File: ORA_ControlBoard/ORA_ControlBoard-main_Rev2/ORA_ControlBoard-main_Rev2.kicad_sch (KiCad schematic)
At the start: 69 parts, among them J1 SM04B-GHS-TB, J2 Conn_01x04_Pin, J3 USB_B_Micro, J4 12V, J5 SM04B-GHS-TB, J6 Conn_02x03_Top_Bottom, J7 Conn_01x05_Pin, J8 Conn_01x05_Pin, J9 Stack Light, Q1 BS170, Q2 IRF9540N, Q3 BS170, Q4 IRF9540N, Q5 BS170, Q6 IRF9540N, SW1 Reset, U1 ATmega32U4-A, U2 MCP25625-x-SS, U5 NCP1117-5.0_SOT223, U6 IMU_MOUNT, Y1 8Mhz, Y2 16MHz

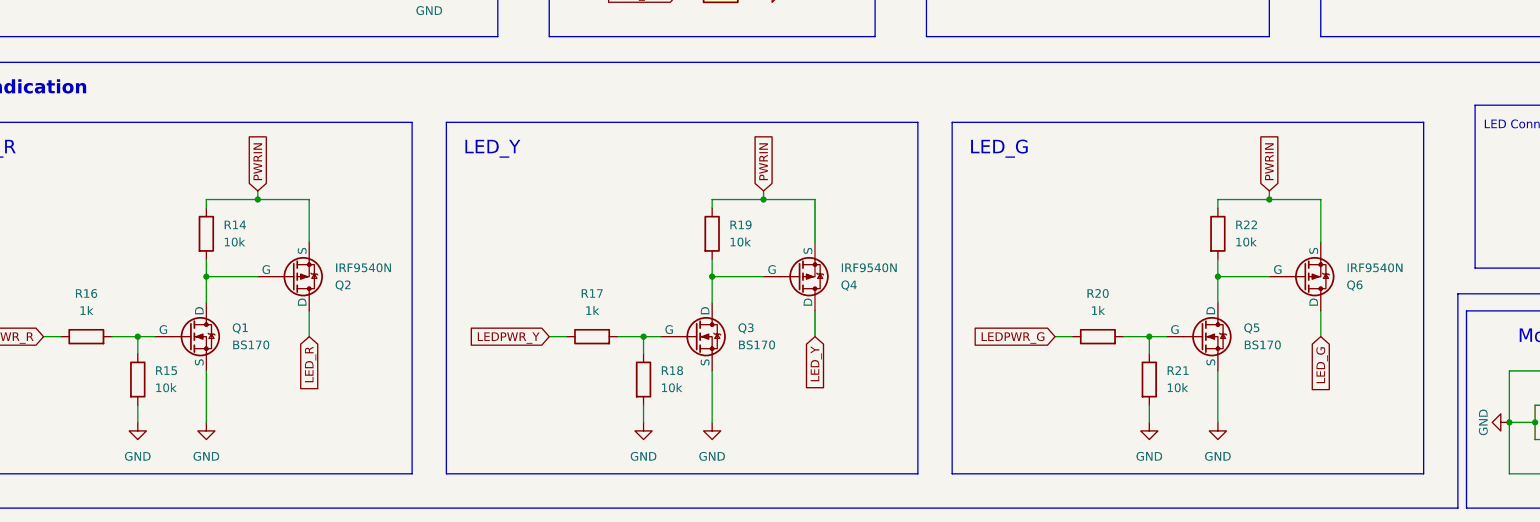
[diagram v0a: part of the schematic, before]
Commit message: Updated LED circuit
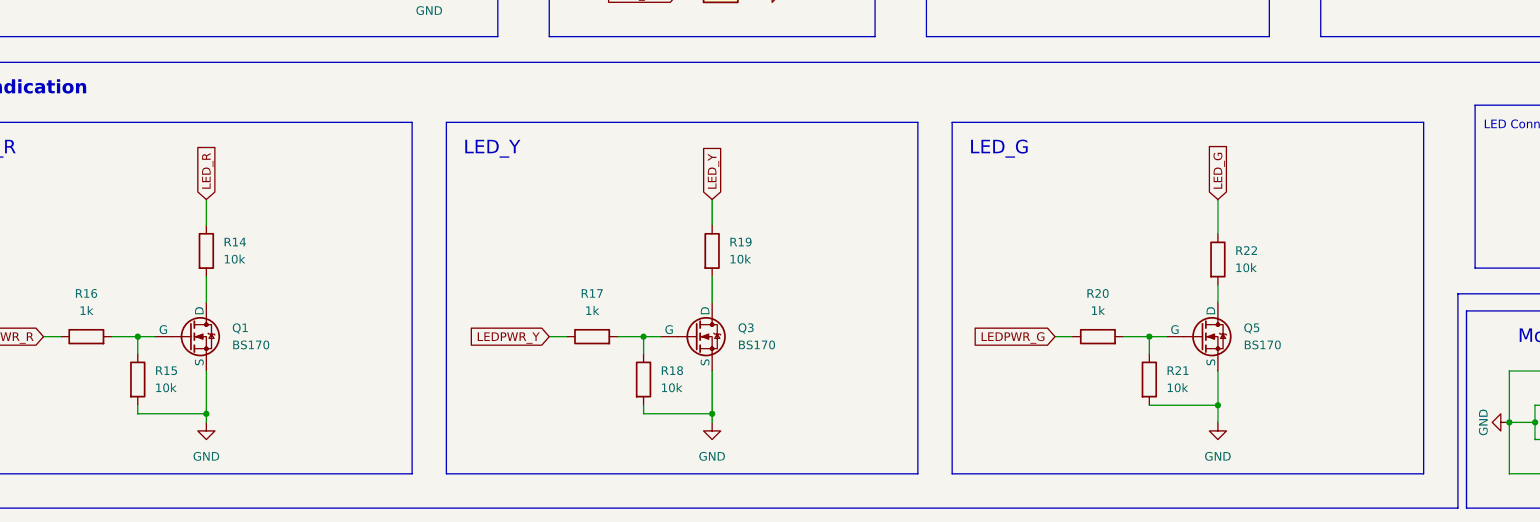
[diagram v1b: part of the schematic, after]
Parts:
- removed Q2, Q4, Q6: IRF9540N, Package_TO_SOT_THT:TO-220-3_Vertical, symbol Simulation_SPICE:PMOS
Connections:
- net LED_G: now also R22.1
- net LED_R: now also R14.1
- net LED_Y: now also R19.1
- net PWRIN: no longer R14.1, R19.1, R22.1
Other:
- moved on the sheet: R14, R19, R22

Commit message: Fixed Spring Cleaning
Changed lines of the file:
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@@
 	(wire
 		(pts
+			(xy 187.96 140.97) (xy 193.04 140.97)
+		)
+		(stroke
+			(width 0)
+			(type default)
+		)
+	)
+	(wire
+		(pts
 			(xy 287.02 101.6) (xy 280.67 101.6)
 		)
@@
 	(wire
 		(pts
+			(xy 187.96 138.43) (xy 193.04 138.43)
+		)
+		(stroke
+			(width 0)
+			(type default)
+		)
+	)
+	(wire
+		(pts
 			(xy 54.61 213.36) (xy 54.61 214.63)
 		)
@@
 	(wire
 		(pts
+			(xy 187.96 135.89) (xy 193.04 135.89)
+		)
+		(stroke
+			(width 0)
+			(type default)
+		)
+	)
+	(wire
+		(pts
 			(xy 266.7 78.74) (xy 262.89 78.74)
 		)
@@
 	(global_label "PWRIN"
 		(shape input)
-		(at 193.04 135.89 180)
+		(at 187.96 135.89 180)
 		(fields_autoplaced yes)
 		(effects
@@
 		)
 		(property "Intersheetrefs" "${INTERSHEET_REFS}"
-			(at 184.1281 135.89 0)
+			(at 179.0481 135.89 0)
 			(effects
 				(font
@@
 	(global_label "CAN_L"
 		(shape input)
-		(at 193.04 140.97 180)
+		(at 187.96 140.97 180)
 		(fields_autoplaced yes)
 		(effects
@@
 		)
 		(property "Intersheetrefs" "${INTERSHEET_REFS}"
-			(at 184.37 140.97 0)
+			(at 179.29 140.97 0)
 			(effects
 				(font
@@
 	(global_label "CAN_H"
 		(shape input)
-		(at 193.04 138.43 180)
+		(at 187.96 138.43 180)
 		(fields_autoplaced yes)
 		(effects
@@
 		)
 		(property "Intersheetrefs" "${INTERSHEET_REFS}"
-			(at 184.0676 138.43 0)
+			(at 178.9876 138.43 0)
 			(effects
 				(font

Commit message: "Final" Rev 2 changes
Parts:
- removed D5: IMU_LED, LED_SMD:LED_0805_2012Metric_Pad1.15x1.40mm_HandSolder, symbol Device:LED_Small
- removed R7: 470, Resistor_SMD:R_0805_2012Metric_Pad1.20x1.40mm_HandSolder, symbol Device:R_Small
- J3: footprint Connector_USB:USB_Micro-B_Amphenol_10118193-0002LF_Horizontal -> AdditionalParts:AMPHENOL_10118192-0002LF
- renumbered R1 to TR1
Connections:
- net LEDPWR_Y is gone; now on net LEDPWR_G: R17.1, U1.26 (PD6)
- net LED_Y is gone; now on net LED_G: J9.3 (Pin_3), R19.1
- net +5V: now also C7.1, U1.7 (VBUS)
- net GND: no longer J9.1 (Pin_1)
- net LEDPWR_G: no longer R20.1, U1.27 (PD7)
- net LED_G: no longer J9.2 (Pin_2), R22.1
- net LED_R: now also J9.2 (Pin_2); no longer J9.4 (Pin_4)
- net PWRIN: now also J9.1 (Pin_1)
- net at D3.2 (A), F1.2: no longer J3.1 (VBUS)
- removed net VBUS: C7.1, F1.1, U1.7 (VBUS)
- new net: F1.1, J3.1 (VBUS)
- new net LEDPWR_B: R20.1, U1.27 (PD7)
- new net LED_B: J9.4 (Pin_4), R22.1
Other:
- note added: "LED_B"
- note removed: "LED_Y"
- moved on the sheet: C11, C12, C13, C14, D3, D4, J3, J4, Q1, Q3, Q5, R14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

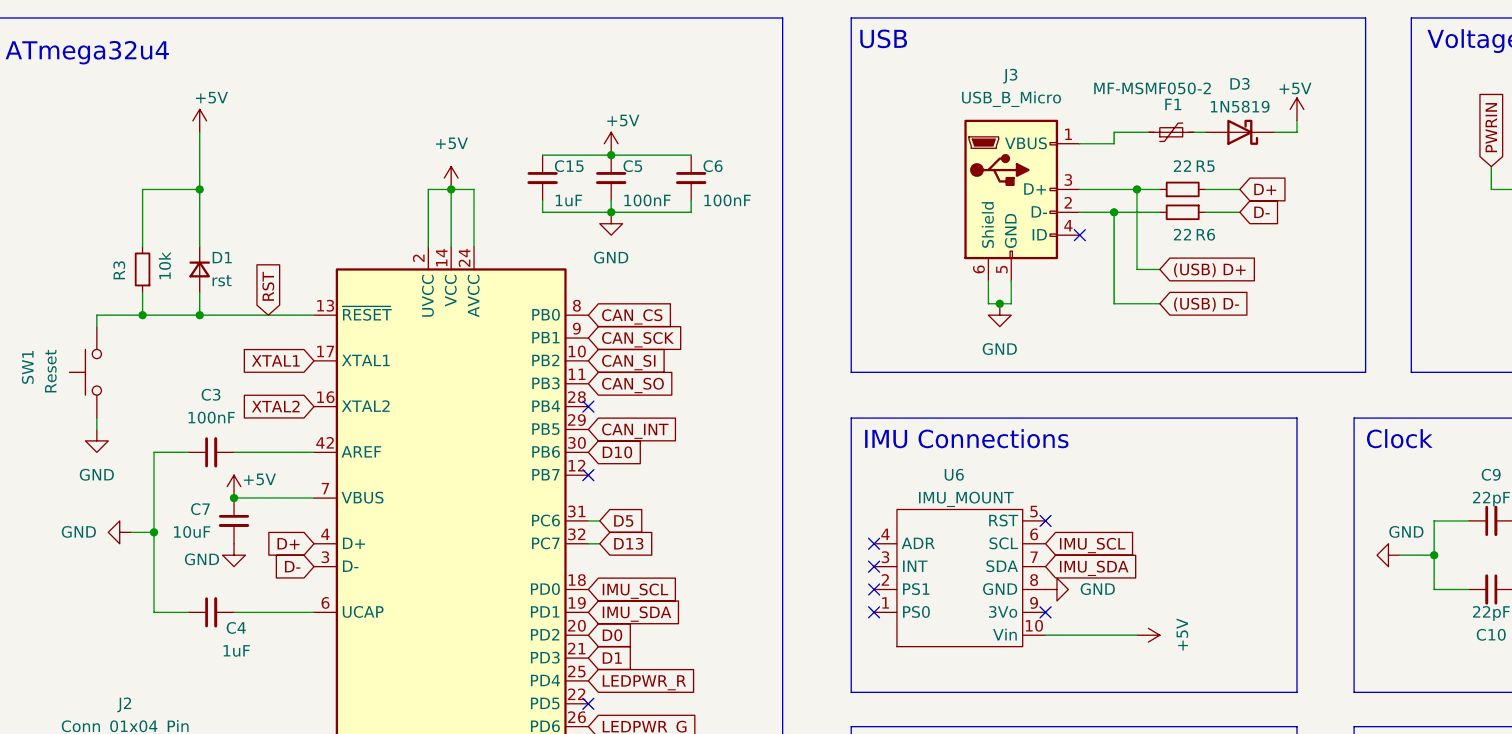
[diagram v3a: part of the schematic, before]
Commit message: Revision
Things changed:
VBUS flag added in between fuse and schottky diode (check this)
Got rid of C7 and GND to VBUS pin on ATmega
Changed silkscreen for ISP pins
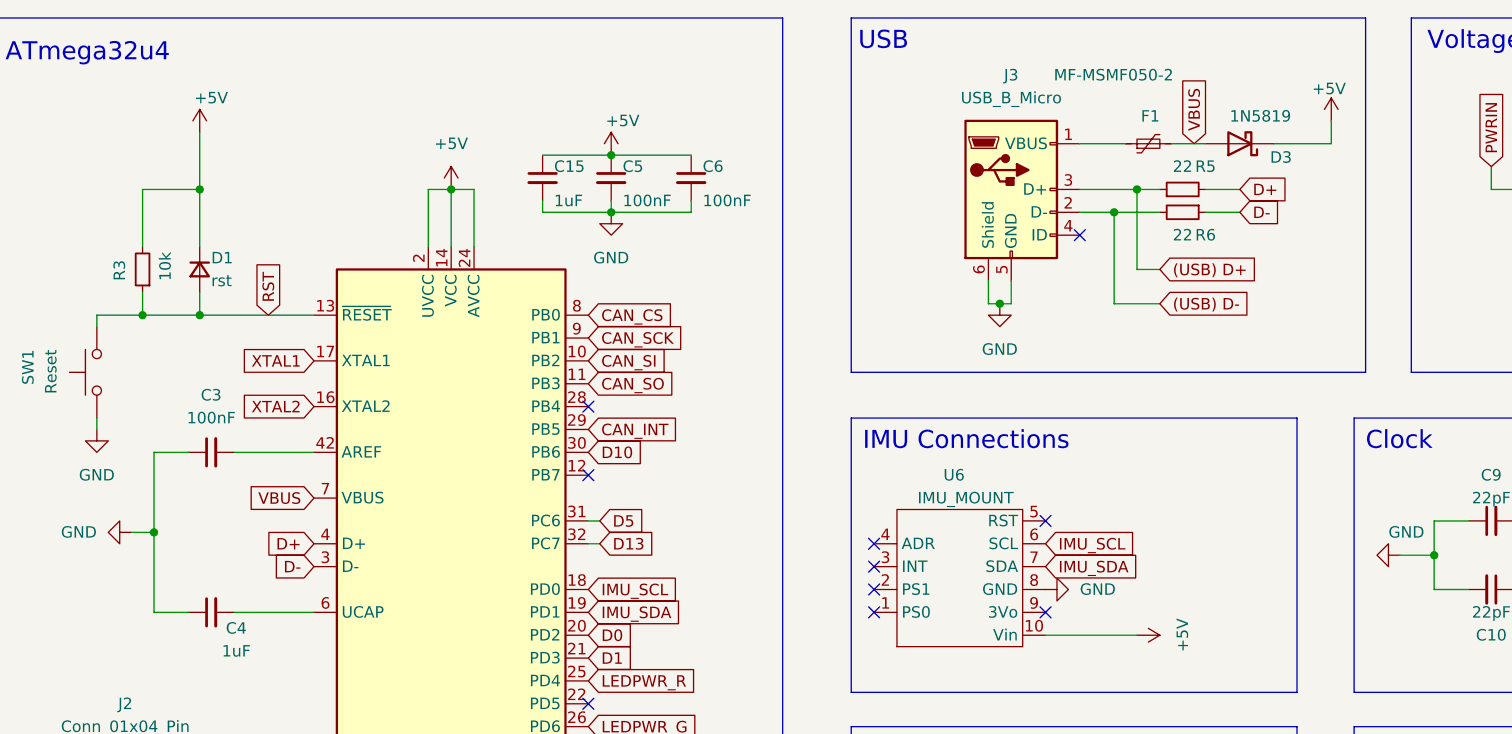
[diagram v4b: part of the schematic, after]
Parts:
- removed C7: 10uF, Capacitor_SMD:C_0805_2012Metric_Pad1.18x1.45mm_HandSolder, symbol Device:C_Small
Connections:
- net +5V: no longer U1.7 (VBUS)
- net VBUS: now reaches D3.2 (A), F1.2
- net VBUS: now also U1.7 (VBUS)
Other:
- moved on the sheet: D3, F1

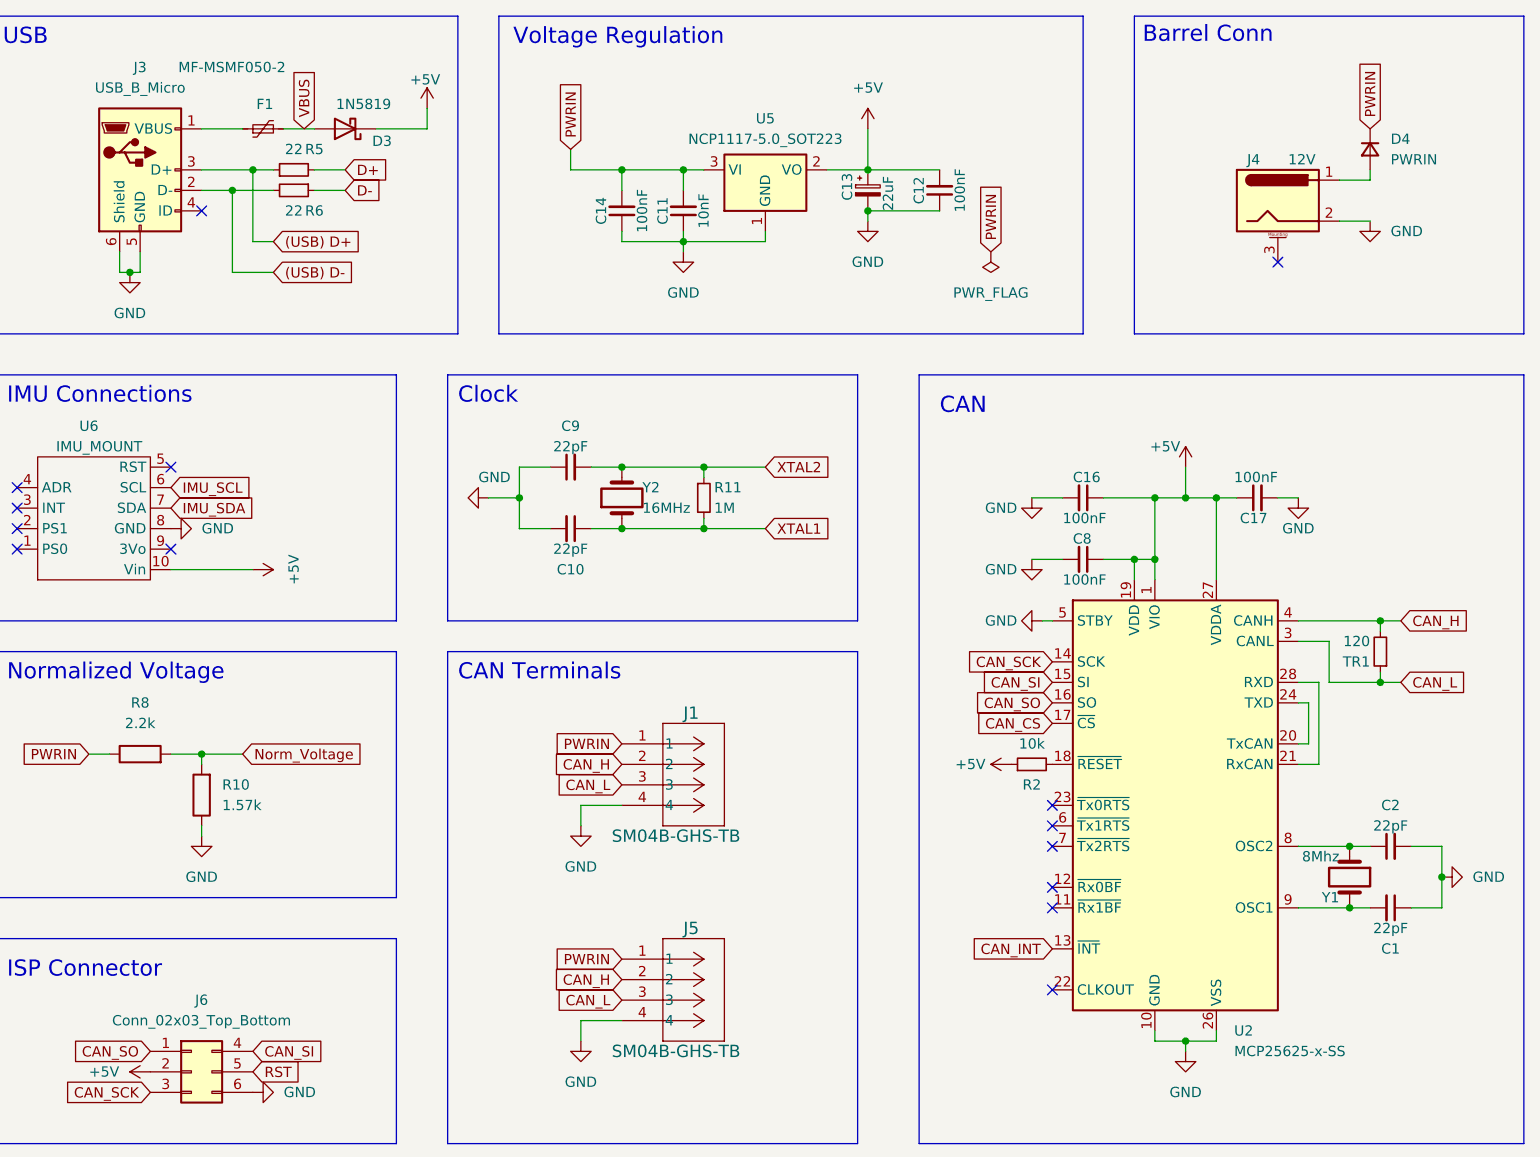
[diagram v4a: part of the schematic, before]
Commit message: Rev 2.1
Things changed:
VBUS flag added in between fuse and schottky diode

Got rid of C7 and GND to VBUS pin on ATmega

Make CAN_H and CAN_L traces differential pairs
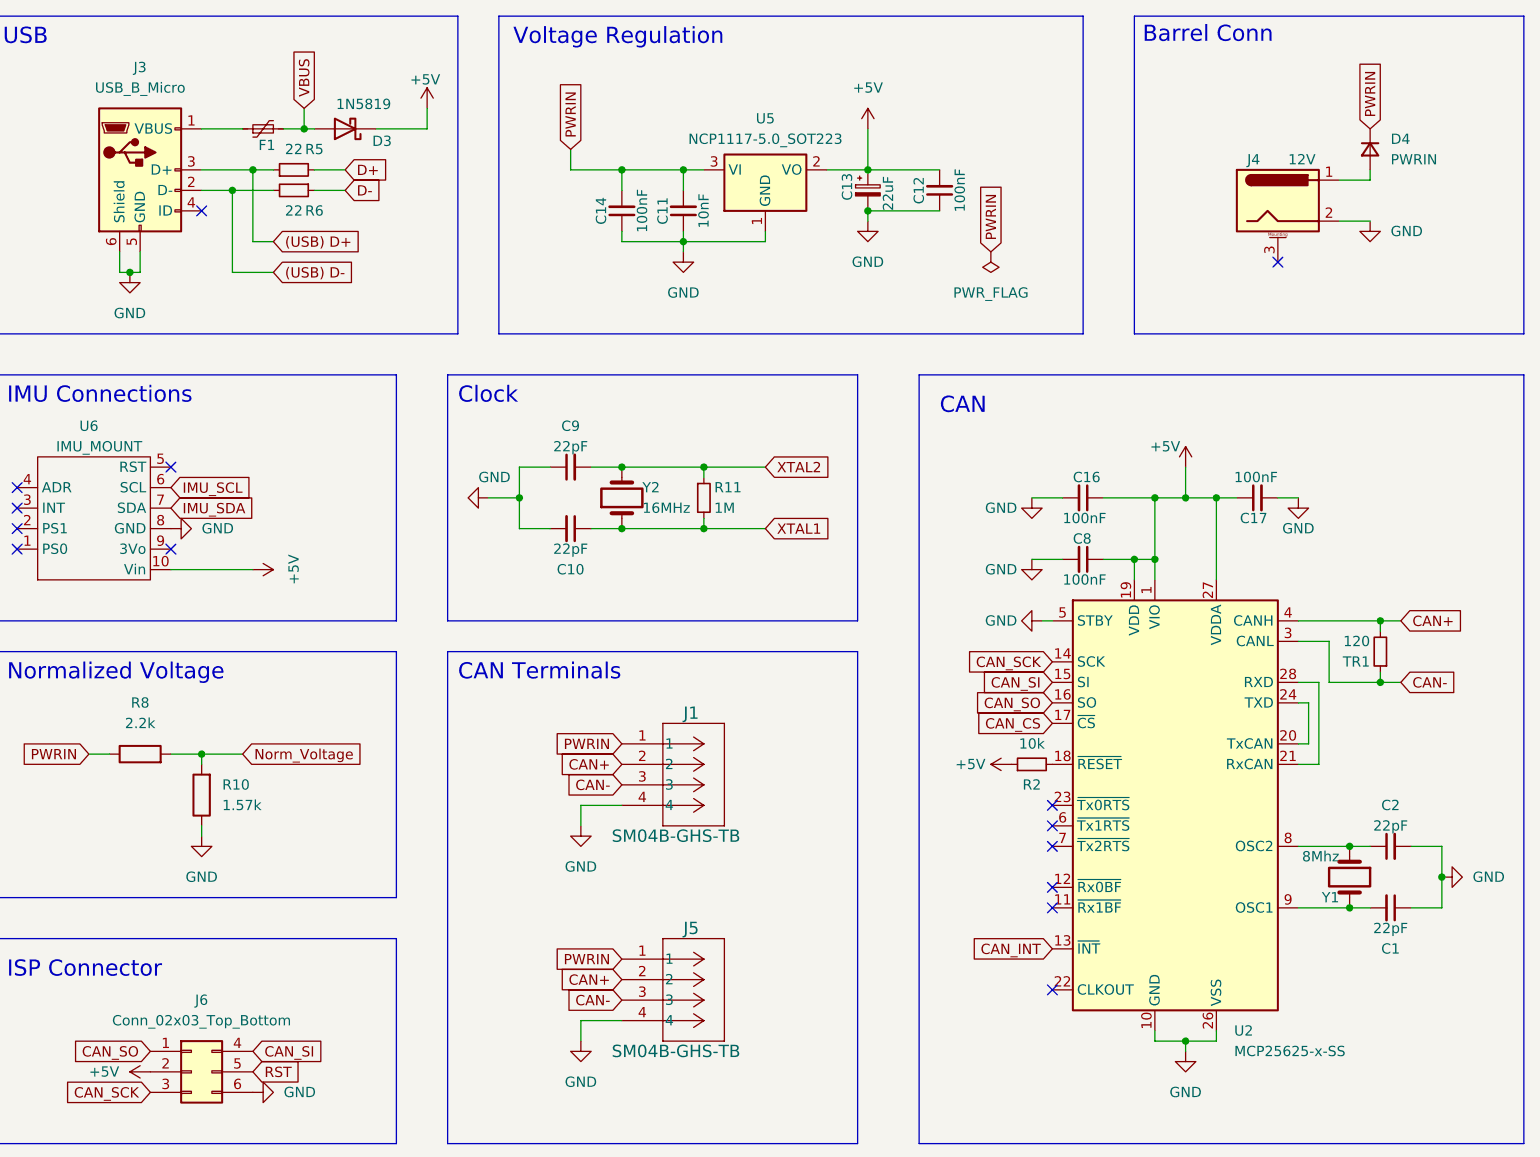
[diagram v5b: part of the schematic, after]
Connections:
- net CAN_H renamed CAN+
- net CAN_L renamed CAN-
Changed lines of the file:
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@@
 	)
 	(junction
+		(at 153.67 33.02)
+		(diameter 0)
+		(color 0 0 0 0)
+	)
+	(junction
 		(at 283.21 121.92)
 		(diameter 0)
@@
 	(wire
 		(pts
+			(xy 153.67 33.02) (xy 154.94 33.02)
+		)
+		(stroke
+			(width 0)
+			(type default)
+		)
+	)
+	(wire
+		(pts
 			(xy 68.58 138.43) (xy 69.85 138.43)
 		)
@@
 	(wire
 		(pts
+			(xy 151.13 33.02) (xy 153.67 33.02)
+		)
+		(stroke
+			(width 0)
+			(type default)
+		)
+	)
+	(wire
+		(pts
 			(xy 276.86 104.14) (xy 278.13 104.14)
 		)
@@
 	(wire
 		(pts
+			(xy 153.67 30.48) (xy 153.67 33.02)
+		)
+		(stroke
+			(width 0)
+			(type default)
+		)
+	)
+	(wire
+		(pts
 			(xy 223.52 33.02) (xy 223.52 38.1)
 		)
@@
 	(wire
 		(pts
-			(xy 151.13 33.02) (xy 154.94 33.02)
-		)
-		(stroke
-			(width 0)
-			(type default)
-		)
-	)
-	(wire
-		(pts
 			(xy 180.34 82.55) (xy 184.15 82.55)
 		)
@@
 	(global_label "VBUS"
 		(shape input)
-		(at 153.67 33.02 90)
+		(at 153.67 30.48 90)
 		(fields_autoplaced yes)
 		(effects
@@
 		)
 		(property "Intersheetrefs" "${INTERSHEET_REFS}"
-			(at 153.67 25.1362 90)
+			(at 153.67 22.5962 90)
 			(effects
 				(font
@@
 		)
 	)
-	(global_label "CAN_H"
+	(global_label "CAN+"
 		(shape input)
 		(at 193.04 111.76 180)
@@
 		)
 		(property "Intersheetrefs" "${INTERSHEET_REFS}"
-			(at 184.0676 111.76 0)
+			(at 184.7933 111.76 0)
 			(effects
 				(font
@@
 		)
 	)
-	(global_label "CAN_L"
+	(global_label "CAN-"
 		(shape input)
 		(at 289.56 101.6 0)
@@
 		)
 		(property "Intersheetrefs" "${INTERSHEET_REFS}"
-			(at 298.23 101.6 0)
+			(at 297.8067 101.6 0)
 			(effects
 				(font
@@
 		)
 	)
-	(global_label "CAN_L"
+	(global_label "CAN-"
 		(shape input)
 		(at 193.04 114.3 180)
@@
 		)
 		(property "Intersheetrefs" "${INTERSHEET_REFS}"
-			(at 184.37 114.3 0)
+			(at 184.7933 114.3 0)
 			(effects
 				(font
@@
 		)
 	)
-	(global_label "CAN_L"
+	(global_label "CAN-"
 		(shape input)
 		(at 193.04 140.97 180)
@@
 		)
 		(property "Intersheetrefs" "${INTERSHEET_REFS}"
-			(at 184.37 140.97 0)
+			(at 184.7933 140.97 0)
 			(effects
 				(font
@@
 		)
 	)
-	(global_label "CAN_H"
+	(global_label "CAN+"
 		(shape input)
 		(at 289.56 93.98 0)
@@
 		)
 		(property "Intersheetrefs" "${INTERSHEET_REFS}"
-			(at 298.5324 93.98 0)
+			(at 297.8067 93.98 0)
 			(effects
 				(font
@@
 		)
 	)
-	(global_label "CAN_H"
+	(global_label "CAN+"
 		(shape input)
 		(at 193.04 138.43 180)
@@
 		)
 		(property "Intersheetrefs" "${INTERSHEET_REFS}"
-			(at 184.0676 138.43 0)
+			(at 184.7933 138.43 0)
 			(effects
 				(font
@@
 		(dnp no)
 		(property "Reference" "F1"
-			(at 149.86 29.972 90)
+			(at 150.114 35.052 90)
 			(effects
 				(font
@@
 		)
 		(property "Value" "MF-MSMF050-2"
-			(at 151.384 25.4 90)
+			(at 156.718 37.084 90)
 			(effects
 				(font
@@
 				)
 				(justify left)
+				(hide yes)
 			)
 		)
